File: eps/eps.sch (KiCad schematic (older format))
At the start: 0 parts

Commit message: fourteen mosfets
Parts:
- added H1: EPS Stack Header 2, symbol Connector_Generic:Conn_02x26_Odd_Even
- added H2: EPS Stack Header 1, symbol Connector_Generic:Conn_02x26_Odd_Even
- added Q1, Q10, Q11, Q12, Q13, Q14, Q2, Q3, Q4, Q5, Q6, Q7, Q8, Q9: IRF7404, Package_SO:SOIC-8_3.9x4.9mm_P1.27mm, symbol Transistor_FET:IRF7404
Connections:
- net +12V: now also Q1.5 (D), Q1.6 (D), Q1.7 (D), Q1.8 (D), Q14.5 (D), Q14.6 (D), Q14.7 (D), Q14.8 (D), Q2.5 (D), Q2.6 (D), Q2.7 (D), Q2.8 (D)
- net +3V3: now also Q10.5 (D), Q10.6 (D), Q10.7 (D), Q10.8 (D), Q11.5 (D), Q11.6 (D), Q11.7 (D), Q11.8 (D), Q8.5 (D), Q8.6 (D), Q8.7 (D), Q8.8 (D), Q9.5 (D), Q9.6 (D), Q9.7 (D), Q9.8 (D)
- net +5V: now also Q12.5 (D), Q12.6 (D), Q12.7 (D), Q12.8 (D), Q5.5 (D), Q5.6 (D), Q5.7 (D), Q5.8 (D), Q6.5 (D), Q6.6 (D), Q6.7 (D), Q6.8 (D), Q7.5 (D), Q7.6 (D), Q7.7 (D), Q7.8 (D)
- net +BATT: now also Q13.5 (D), Q13.6 (D), Q13.7 (D), Q13.8 (D), Q3.5 (D), Q3.6 (D), Q3.7 (D), Q3.8 (D), Q4.5 (D), Q4.6 (D), Q4.7 (D), Q4.8 (D)
- net GND: now also H2.14 (Pin_14), H2.17 (Pin_17), H2.21 (Pin_21), H2.22 (Pin_22), H2.29 (Pin_29), H2.30 (Pin_30), H2.32 (Pin_32), H2.47 (Pin_47), H2.48 (Pin_48), H2.9 (Pin_9)
- new net 12VBUS: H2.23 (Pin_23), H2.24 (Pin_24), Q14.1 (S), Q14.2 (S), Q14.3 (S)
- new net 3V3BUS: H2.27 (Pin_27), H2.28 (Pin_28), Q11.1 (S), Q11.2 (S), Q11.3 (S)
- new net 5VBUS: H2.25 (Pin_25), H2.26 (Pin_26), Q12.1 (S), Q12.2 (S), Q12.3 (S)
- new net 5VUSBCHG: H1.32 (Pin_32)
- new net BATTBUS: H2.45 (Pin_45), H2.46 (Pin_46), Q13.1 (S), Q13.2 (S), Q13.3 (S)
- new net BCR_OUT: H2.41 (Pin_41), H2.42 (Pin_42), H2.43 (Pin_43), H2.44 (Pin_44)
- new net BUS12SIG: Q14.4 (G)
- new net BUS3SIG: Q11.4 (G)
- new net BUS5SIG: Q12.4 (G)
- new net BUSBSIG: Q13.4 (G)
- new net PCM_IN: H2.35 (Pin_35), H2.36 (Pin_36)
- new net SCL: H1.43 (Pin_43)
- new net SDA: H1.41 (Pin_41)
- new net SIG1: Q1.4 (G)
- new net SIG10: Q10.4 (G)
- new net SIG2: Q2.4 (G)
- new net SIG3: Q3.4 (G)
- new net SIG4: Q4.4 (G)
- new net SIG5: Q5.4 (G)
- new net SIG6: Q6.4 (G)
- new net SIG7: Q7.4 (G)
- new net SIG8: Q8.4 (G)
- new net SIG9: Q9.4 (G)
- new net SW1: H2.8 (Pin_8), Q1.1 (S), Q1.2 (S), Q1.3 (S)
- new net SW10: H2.20 (Pin_20), Q10.1 (S), Q10.2 (S), Q10.3 (S)
- new net SW2: H2.10 (Pin_10), Q2.1 (S), Q2.2 (S), Q2.3 (S)
- new net SW3: H2.11 (Pin_11), Q3.1 (S), Q3.2 (S), Q3.3 (S)
- new net SW4: H2.12 (Pin_12), Q4.1 (S), Q4.2 (S), Q4.3 (S)
- new net SW5: H2.13 (Pin_13), Q5.1 (S), Q5.2 (S), Q5.3 (S)
- new net SW6: H2.15 (Pin_15), Q6.1 (S), Q6.2 (S), Q6.3 (S)
- new net SW7: H2.16 (Pin_16), Q7.1 (S), Q7.2 (S), Q7.3 (S)
- new net SW8: H2.18 (Pin_18), Q8.1 (S), Q8.2 (S), Q8.3 (S)
- new net SW9: H2.19 (Pin_19), Q9.1 (S), Q9.2 (S), Q9.3 (S)
- no-connect marks 0 -> 67
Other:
- note added: "FOURTEEN MOSFETS!!!!!"

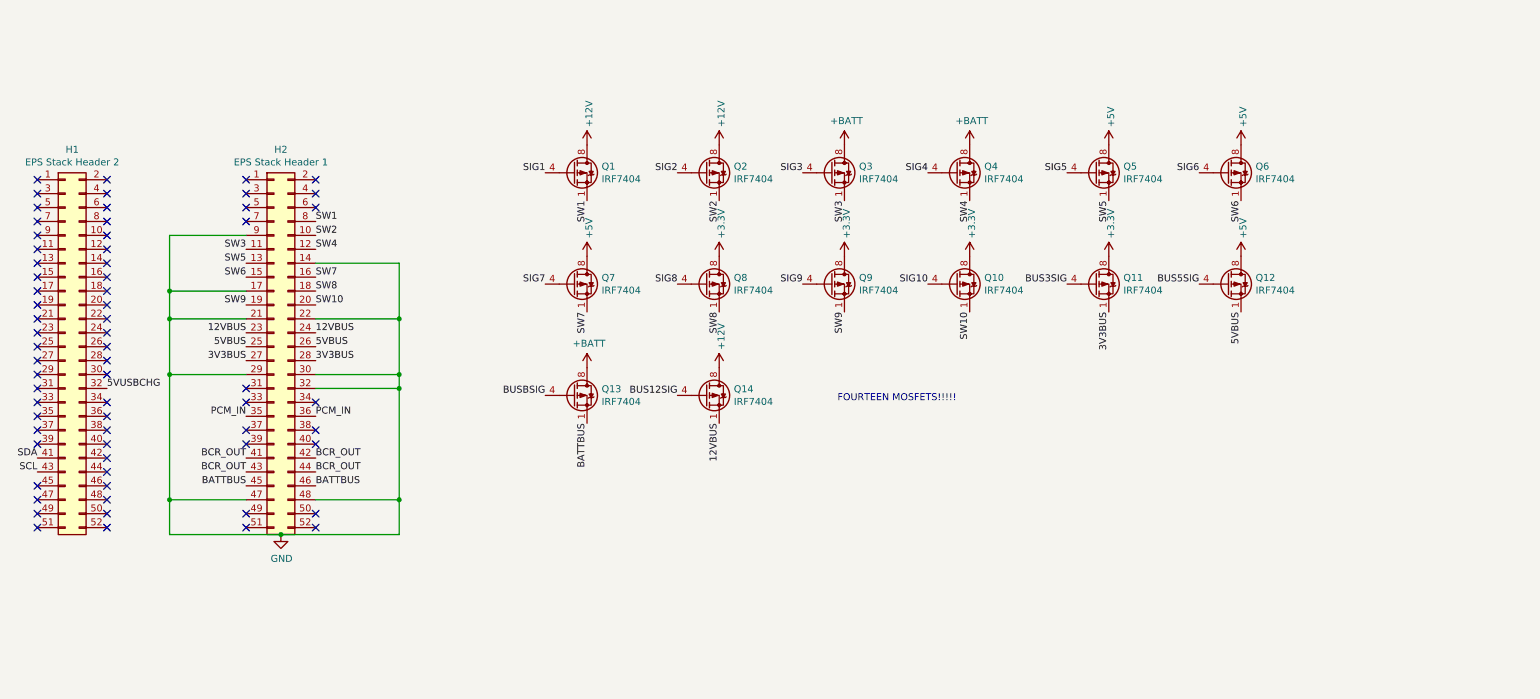
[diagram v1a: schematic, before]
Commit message: 24 mosfets
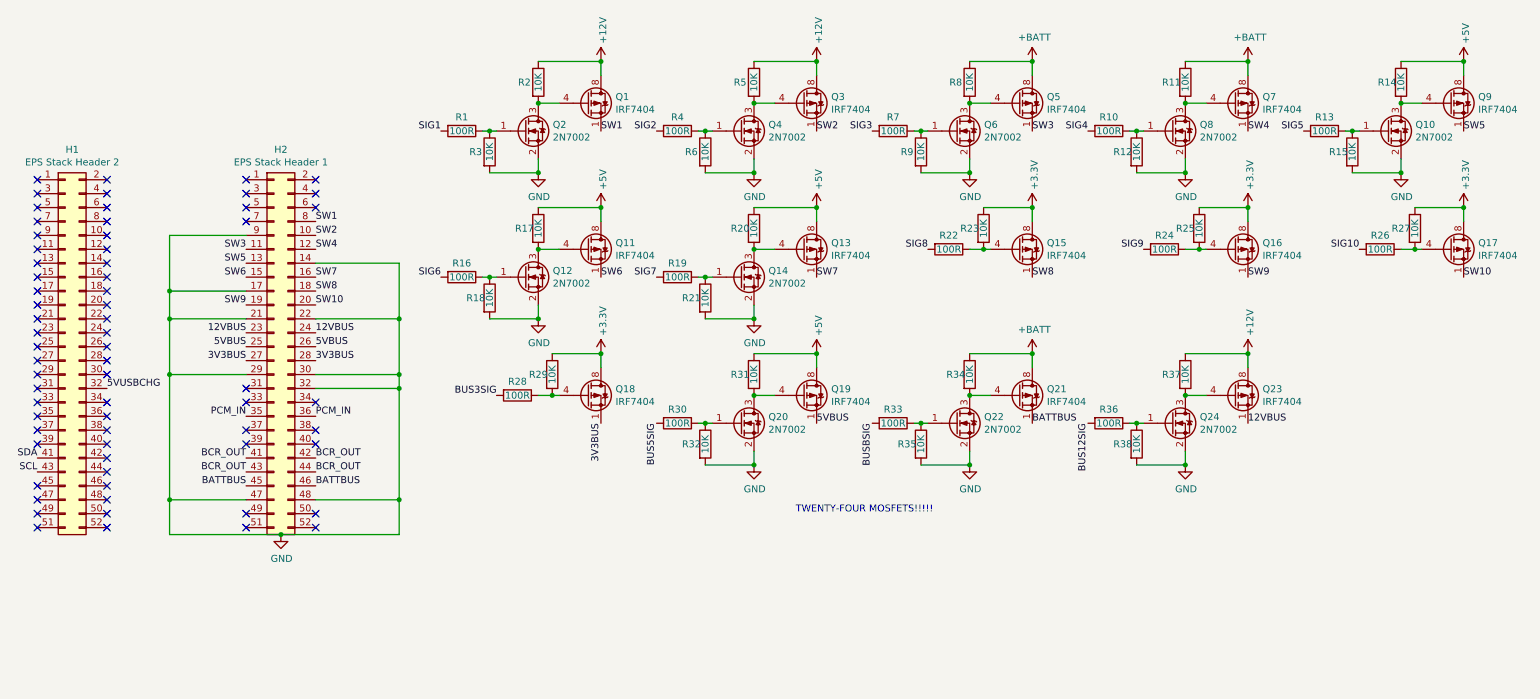
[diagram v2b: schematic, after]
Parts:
- removed Q10, Q12, Q14, Q2, Q4, Q6, Q8: IRF7404, Package_SO:SOIC-8_3.9x4.9mm_P1.27mm, symbol Transistor_FET:IRF7404
- added Q10, Q12, Q14, Q2, Q20, Q22, Q24, Q4, Q6, Q8: 2N7002, Package_TO_SOT_SMD:SOT-23, symbol Transistor_FET:2N7002
- added Q11, Q15, Q16, Q17, Q19, Q21, Q23: IRF7404, Package_SO:SOIC-8_3.9x4.9mm_P1.27mm, symbol Transistor_FET:IRF7404
- added R1, R10, R13, R16, R19, R22, R24, R26, R28, R30, R33, R36, R4, R7: 100R, symbol Device:R
- added R11, R12, R14, R15, R17, R18, R2, R20, R21, R23, R25, R27, R29, R3, R31, R32, R34, R35, R37, R38, R5, R6, R8, R9: 10K, symbol Device:R
- renumbered Q11 to Q18
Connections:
- net +12V: now also Q3.5 (D), Q3.6 (D), Q3.7 (D), Q3.8 (D), Q23.5 (D), Q23.6 (D), Q23.7 (D), Q23.8 (D), R2.1, R37.1, R5.1
- net +3V3: now also Q15.5 (D), Q15.6 (D), Q15.7 (D), Q15.8 (D), Q16.5 (D), Q16.6 (D), Q16.7 (D), Q16.8 (D), Q17.5 (D), Q17.6 (D), Q17.7 (D), Q17.8 (D), R23.1, R25.1, R27.1, R29.1; no longer Q9.5 (D), Q9.6 (D), Q9.7 (D), Q9.8 (D)
- net +5V: now also Q13.5 (D), Q13.6 (D), Q13.7 (D), Q13.8 (D), Q9.5 (D), Q9.6 (D), Q9.7 (D), Q9.8 (D), Q11.5 (D), Q11.6 (D), Q11.7 (D), Q11.8 (D), Q19.5 (D), Q19.6 (D), Q19.7 (D), Q19.8 (D), R14.1, R17.1, R20.1, R31.1; no longer Q5.5 (D), Q5.6 (D), Q5.7 (D), Q5.8 (D), Q7.5 (D), Q7.6 (D), Q7.7 (D), Q7.8 (D)
- net +BATT: now also Q5.5 (D), Q5.6 (D), Q5.7 (D), Q5.8 (D), Q7.5 (D), Q7.6 (D), Q7.7 (D), Q7.8 (D), Q21.5 (D), Q21.6 (D), Q21.7 (D), Q21.8 (D), R11.1, R34.1, R8.1; no longer Q13.5 (D), Q13.6 (D), Q13.7 (D), Q13.8 (D), Q3.5 (D), Q3.6 (D), Q3.7 (D), Q3.8 (D)
- net 12VBUS: now also Q23.1 (S), Q23.2 (S), Q23.3 (S)
- net 5VBUS: now also Q19.1 (S), Q19.2 (S), Q19.3 (S)
- net BATTBUS: now also Q21.1 (S), Q21.2 (S), Q21.3 (S); no longer Q13.1 (S), Q13.2 (S), Q13.3 (S)
- net BUS12SIG: now also R36.2
- net BUS3SIG: now also R28.2; no longer Q18.4 (G)
- net BUS5SIG: now also R30.2
- net BUSBSIG: now also R33.2; no longer Q13.4 (G)
- net GND: now also Q10.2 (S), Q12.2 (S), Q14.2 (S), Q2.2 (S), Q20.2 (S), Q22.2 (S), Q24.2 (S), Q4.2 (S), Q6.2 (S), Q8.2 (S), R12.2, R15.2, R18.2, R21.2, R3.2, R32.2, R35.2, R38.2, R6.2, R9.2
- net SIG1: now also R1.2; no longer Q1.4 (G)
- net SIG10: now also R26.2
- net SIG2: now also R4.2
- net SIG3: now also R7.2; no longer Q3.4 (G)
- net SIG4: now also R10.2
- net SIG5: now also R13.2; no longer Q5.4 (G)
- net SIG6: now also R16.2
- net SIG7: now also R19.2; no longer Q7.4 (G)
- net SIG8: now also R22.2
- net SIG9: now also R24.2; no longer Q9.4 (G)
- net SW10: now also Q17.1 (S), Q17.2 (S), Q17.3 (S)
- net SW2: now also Q3.1 (S), Q3.2 (S), Q3.3 (S)
- net SW3: now also Q5.1 (S), Q5.2 (S), Q5.3 (S); no longer Q3.1 (S), Q3.2 (S), Q3.3 (S)
- net SW4: now also Q7.1 (S), Q7.2 (S), Q7.3 (S)
- net SW5: now also Q9.1 (S), Q9.2 (S), Q9.3 (S); no longer Q5.1 (S), Q5.2 (S), Q5.3 (S)
- net SW6: now also Q11.1 (S), Q11.2 (S), Q11.3 (S)
- net SW7: now also Q13.1 (S), Q13.2 (S), Q13.3 (S); no longer Q7.1 (S), Q7.2 (S), Q7.3 (S)
- net SW8: now also Q15.1 (S), Q15.2 (S), Q15.3 (S)
- net SW9: now also Q16.1 (S), Q16.2 (S), Q16.3 (S); no longer Q9.1 (S), Q9.2 (S), Q9.3 (S)
- new net: Q2.1 (G), R1.1, R3.1
- new net: Q1.4 (G), Q2.3 (D), R2.2
- new net: Q18.4 (G), R28.1, R29.2
- new net: Q4.1 (G), R4.1, R6.1
- new net: Q3.4 (G), Q4.3 (D), R5.2
- new net: Q6.1 (G), R7.1, R9.1
- new net: Q5.4 (G), Q6.3 (D), R8.2
- new net: Q8.1 (G), R10.1, R12.1
- new net: Q7.4 (G), Q8.3 (D), R11.2
- new net: Q10.1 (G), R13.1, R15.1
- new net: Q10.3 (D), Q9.4 (G), R14.2
- new net: Q12.1 (G), R16.1, R18.1
- new net: Q11.4 (G), Q12.3 (D), R17.2
- new net: Q14.1 (G), R19.1, R21.1
- new net: Q13.4 (G), Q14.3 (D), R20.2
- new net: Q15.4 (G), R22.1, R23.2
- new net: Q16.4 (G), R24.1, R25.2
- new net: Q17.4 (G), R26.1, R27.2
- new net: Q20.1 (G), R30.1, R32.1
- new net: Q19.4 (G), Q20.3 (D), R31.2
- new net: Q22.1 (G), R33.1, R35.1
- new net: Q21.4 (G), Q22.3 (D), R34.2
- new net: Q24.1 (G), R36.1, R38.1
- new net: Q23.4 (G), Q24.3 (D), R37.2
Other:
- note added: "TWENTY-FOUR MOSFETS!!!!!"
- note removed: "FOURTEEN MOSFETS!!!!!"
- moved on the sheet: Q1, Q18

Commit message: correct p channel orientation, bias bus to be on with no input
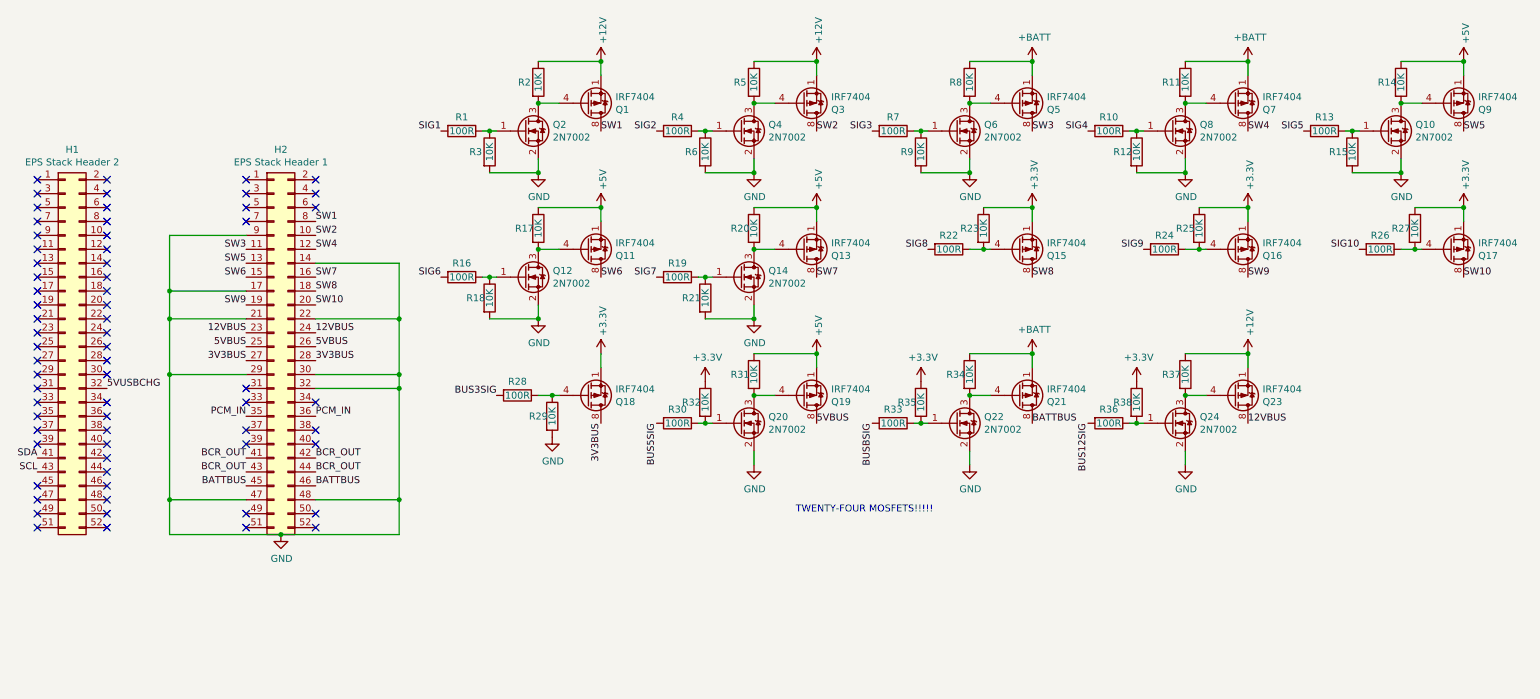
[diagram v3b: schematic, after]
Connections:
- net +12V: now also Q1.1 (S), Q1.2 (S), Q1.3 (S), Q23.1 (S), Q23.2 (S), Q23.3 (S), Q3.1 (S), Q3.2 (S), Q3.3 (S); no longer Q1.5 (D), Q1.6 (D), Q1.7 (D), Q1.8 (D), Q23.5 (D), Q23.6 (D), Q23.7 (D), Q23.8 (D), Q3.5 (D), Q3.6 (D), Q3.7 (D), Q3.8 (D)
- net +3V3: now also Q15.1 (S), Q15.2 (S), Q15.3 (S), Q16.1 (S), Q16.2 (S), Q16.3 (S), Q17.1 (S), Q17.2 (S), Q17.3 (S), Q18.1 (S), Q18.2 (S), Q18.3 (S), R32.1, R35.1, R38.1; no longer Q15.5 (D), Q15.6 (D), Q15.7 (D), Q15.8 (D), Q16.5 (D), Q16.6 (D), Q16.7 (D), Q16.8 (D), Q17.5 (D), Q17.6 (D), Q17.7 (D), Q17.8 (D), Q18.5 (D), Q18.6 (D), Q18.7 (D), Q18.8 (D), R29.1
- net +5V: now also Q11.1 (S), Q11.2 (S), Q11.3 (S), Q13.1 (S), Q13.2 (S), Q13.3 (S), Q19.1 (S), Q19.2 (S), Q19.3 (S), Q9.1 (S), Q9.2 (S), Q9.3 (S); no longer Q11.5 (D), Q11.6 (D), Q11.7 (D), Q11.8 (D), Q13.5 (D), Q13.6 (D), Q13.7 (D), Q13.8 (D), Q19.5 (D), Q19.6 (D), Q19.7 (D), Q19.8 (D), Q9.5 (D), Q9.6 (D), Q9.7 (D), Q9.8 (D)
- net +BATT: now also Q21.1 (S), Q21.2 (S), Q21.3 (S), Q5.1 (S), Q5.2 (S), Q5.3 (S), Q7.1 (S), Q7.2 (S), Q7.3 (S); no longer Q21.5 (D), Q21.6 (D), Q21.7 (D), Q21.8 (D), Q5.5 (D), Q5.6 (D), Q5.7 (D), Q5.8 (D), Q7.5 (D), Q7.6 (D), Q7.7 (D), Q7.8 (D)
- net 12VBUS: now also Q23.5 (D), Q23.6 (D), Q23.7 (D), Q23.8 (D); no longer Q23.1 (S), Q23.2 (S), Q23.3 (S)
- net 3V3BUS: now also Q18.5 (D), Q18.6 (D), Q18.7 (D), Q18.8 (D); no longer Q18.1 (S), Q18.2 (S), Q18.3 (S)
- net 5VBUS: now also Q19.5 (D), Q19.6 (D), Q19.7 (D), Q19.8 (D); no longer Q19.1 (S), Q19.2 (S), Q19.3 (S)
- net BATTBUS: now also Q21.5 (D), Q21.6 (D), Q21.7 (D), Q21.8 (D); no longer Q21.1 (S), Q21.2 (S), Q21.3 (S)
- net GND: now also R29.2; no longer R32.2, R35.2, R38.2
- net SW1: now also Q1.5 (D), Q1.6 (D), Q1.7 (D), Q1.8 (D); no longer Q1.1 (S), Q1.2 (S), Q1.3 (S)
- net SW10: now also Q17.5 (D), Q17.6 (D), Q17.7 (D), Q17.8 (D); no longer Q17.1 (S), Q17.2 (S), Q17.3 (S)
- net SW2: now also Q3.5 (D), Q3.6 (D), Q3.7 (D), Q3.8 (D); no longer Q3.1 (S), Q3.2 (S), Q3.3 (S)
- net SW3: now also Q5.5 (D), Q5.6 (D), Q5.7 (D), Q5.8 (D); no longer Q5.1 (S), Q5.2 (S), Q5.3 (S)
- net SW4: now also Q7.5 (D), Q7.6 (D), Q7.7 (D), Q7.8 (D); no longer Q7.1 (S), Q7.2 (S), Q7.3 (S)
- net SW5: now also Q9.5 (D), Q9.6 (D), Q9.7 (D), Q9.8 (D); no longer Q9.1 (S), Q9.2 (S), Q9.3 (S)
- net SW6: now also Q11.5 (D), Q11.6 (D), Q11.7 (D), Q11.8 (D); no longer Q11.1 (S), Q11.2 (S), Q11.3 (S)
- net SW7: now also Q13.5 (D), Q13.6 (D), Q13.7 (D), Q13.8 (D); no longer Q13.1 (S), Q13.2 (S), Q13.3 (S)
- net SW8: now also Q15.5 (D), Q15.6 (D), Q15.7 (D), Q15.8 (D); no longer Q15.1 (S), Q15.2 (S), Q15.3 (S)
- net SW9: now also Q16.5 (D), Q16.6 (D), Q16.7 (D), Q16.8 (D); no longer Q16.1 (S), Q16.2 (S), Q16.3 (S)
- net at Q18.4 (G), R28.1: now also R29.1; no longer R29.2
- net at Q20.1 (G), R30.1: now also R32.2; no longer R32.1
- net at Q22.1 (G), R33.1: now also R35.2; no longer R35.1
- net at Q24.1 (G), R36.1: now also R38.2; no longer R38.1
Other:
- moved on the sheet: R29, R32, R35, R38
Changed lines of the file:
@@
 F 3 "http://www.infineon.com/dgdl/irf7404.pdf?fileId=5546d462533600a4015355fa2b5b1b9e" V 4700 3200 50  0001 L CNN
 	1    4700 3200
-	1    0    0    -1
+	1    0    0    1
 $EndComp
 Text Label 3650 1300 2    50   ~ 0
@@
 F 3 "http://www.infineon.com/dgdl/irf7404.pdf?fileId=5546d462533600a4015355fa2b5b1b9e" V 4700 1100 50  0001 L CNN
 	1    4700 1100
-	1    0    0    -1
+	1    0    0    1
 $EndComp
 $Comp
@@
 F 3 "http://www.infineon.com/dgdl/irf7404.pdf?fileId=5546d462533600a4015355fa2b5b1b9e" V 6250 1100 50  0001 L CNN
 	1    6250 1100
-	1    0    0    -1
+	1    0    0    1
 $EndComp
 $Comp
@@
 F 3 "http://www.infineon.com/dgdl/irf7404.pdf?fileId=5546d462533600a4015355fa2b5b1b9e" V 7800 1100 50  0001 L CNN
 	1    7800 1100
-	1    0    0    -1
+	1    0    0    1
 $EndComp
 $Comp
@@
 F 3 "http://www.infineon.com/dgdl/irf7404.pdf?fileId=5546d462533600a4015355fa2b5b1b9e" V 9350 1100 50  0001 L CNN
 	1    9350 1100
-	1    0    0    -1
+	1    0    0    1
 $EndComp
 $Comp
@@
 F 3 "http://www.infineon.com/dgdl/irf7404.pdf?fileId=5546d462533600a4015355fa2b5b1b9e" V 10900 1100 50  0001 L CNN
 	1    10900 1100
-	1    0    0    -1
+	1    0    0    1
 $EndComp
 $Comp
@@
 F 3 "http://www.infineon.com/dgdl/irf7404.pdf?fileId=5546d462533600a4015355fa2b5b1b9e" V 4700 2150 50  0001 L CNN
 	1    4700 2150
-	1    0    0    -1
+	1    0    0    1
 $EndComp
 $Comp
@@
 F 3 "http://www.infineon.com/dgdl/irf7404.pdf?fileId=5546d462533600a4015355fa2b5b1b9e" V 6250 2150 50  0001 L CNN
 	1    6250 2150
-	1    0    0    -1
+	1    0    0    1
 $EndComp
 $Comp
@@
 F 3 "http://www.infineon.com/dgdl/irf7404.pdf?fileId=5546d462533600a4015355fa2b5b1b9e" V 7800 2150 50  0001 L CNN
 	1    7800 2150
-	1    0    0    -1
+	1    0    0    1
 $EndComp
 Wire Wire Line
@@
 F 3 "http://www.infineon.com/dgdl/irf7404.pdf?fileId=5546d462533600a4015355fa2b5b1b9e" V 9350 2150 50  0001 L CNN
 	1    9350 2150
-	1    0    0    -1
+	1    0    0    1
 $EndComp
 Wire Wire Line
@@
 F 3 "http://www.infineon.com/dgdl/irf7404.pdf?fileId=5546d462533600a4015355fa2b5b1b9e" V 10900 2150 50  0001 L CNN
 	1    10900 2150
-	1    0    0    -1
+	1    0    0    1
 $EndComp
 Wire Wire Line
@@
 L Device:R R29
 U 1 1 6191C4AE
-P 4450 3050
-F 0 "R29" H 4350 3050 50  0000 C CNN
-F 1 "10K" V 4450 3050 50  0000 C CNN
-F 2 "" V 4380 3050 50  0001 C CNN
-F 3 "~" H 4450 3050 50  0001 C CNN
-	1    4450 3050
-	1    0    0    -1
-$EndComp
-Wire Wire Line
-	4450 2900 4800 2900
+P 4450 3350
+F 0 "R29" H 4350 3350 50  0000 C CNN
+F 1 "10K" V 4450 3350 50  0000 C CNN
+F 2 "" V 4380 3350 50  0001 C CNN
+F 3 "~" H 4450 3350 50  0001 C CNN
+	1    4450 3350
+	1    0    0    -1
+$EndComp
 Wire Wire Line
 	4350 3200 4450 3200
@@
 Wire Wire Line
 	4800 2900 4800 3000
-Connection ~ 4800 2900
 $Comp
 L Device:R R30
@@
 F 3 "http://www.infineon.com/dgdl/irf7404.pdf?fileId=5546d462533600a4015355fa2b5b1b9e" V 6250 3200 50  0001 L CNN
 	1    6250 3200
-	1    0    0    -1
+	1    0    0    1
 $EndComp
 $Comp
@@
 L Device:R R32
 U 1 1 61927005
-P 5550 3550
-F 0 "R32" H 5450 3550 50  0000 C CNN
-F 1 "10K" V 5550 3550 50  0000 C CNN
-F 2 "" V 5480 3550 50  0001 C CNN
-F 3 "~" H 5550 3550 50  0001 C CNN
-	1    5550 3550
-	1    0    0    -1
-$EndComp
-Wire Wire Line
-	5550 3700 5900 3700
+P 5550 3250
+F 0 "R32" H 5450 3250 50  0000 C CNN
+F 1 "10K" V 5550 3250 50  0000 C CNN
+F 2 "" V 5480 3250 50  0001 C CNN
+F 3 "~" H 5550 3250 50  0001 C CNN
+	1    5550 3250
+	1    0    0    -1
+$EndComp
 Wire Wire Line
 	5900 3700 5900 3600
-Connection ~ 5900 3700
 Connection ~ 5550 3400
 Wire Wire Line
@@
 F 3 "http://www.infineon.com/dgdl/irf7404.pdf?fileId=5546d462533600a4015355fa2b5b1b9e" V 7800 3200 50  0001 L CNN
 	1    7800 3200
-	1    0    0    -1
+	1    0    0    1
 $EndComp
 $Comp
@@
 L Device:R R35
 U 1 1 6193C026
-P 7100 3550
-F 0 "R35" H 7000 3550 50  0000 C CNN
-F 1 "10K" V 7100 3550 50  0000 C CNN
-F 2 "" V 7030 3550 50  0001 C CNN
-F 3 "~" H 7100 3550 50  0001 C CNN
-	1    7100 3550
-	1    0    0    -1
-$EndComp
-Wire Wire Line
-	7100 3700 7450 3700
+P 7100 3250
+F 0 "R35" H 7000 3250 50  0000 C CNN
+F 1 "10K" V 7100 3250 50  0000 C CNN
+F 2 "" V 7030 3250 50  0001 C CNN
+F 3 "~" H 7100 3250 50  0001 C CNN
+	1    7100 3250
+	1    0    0    -1
+$EndComp
 Wire Wire Line
 	7450 3700 7450 3600
-Connection ~ 7450 3700
 Connection ~ 7100 3400
 Wire Wire Line
@@
 F 3 "http://www.infineon.com/dgdl/irf7404.pdf?fileId=5546d462533600a4015355fa2b5b1b9e" V 9350 3200 50  0001 L CNN
 	1    9350 3200
-	1    0    0    -1
+	1    0    0    1
 $EndComp
 $Comp
@@
 L Device:R R38
 U 1 1 61959E02
-P 8650 3550
-F 0 "R38" H 8550 3550 50  0000 C CNN
-F 1 "10K" V 8650 3550 50  0000 C CNN
-F 2 "" V 8580 3550 50  0001 C CNN
-F 3 "~" H 8650 3550 50  0001 C CNN
-	1    8650 3550
-	1    0    0    -1
-$EndComp
-Wire Wire Line
-	8650 3700 9000 3700
+P 8650 3250
+F 0 "R38" H 8550 3250 50  0000 C CNN
+F 1 "10K" V 8650 3250 50  0000 C CNN
+F 2 "" V 8580 3250 50  0001 C CNN
+F 3 "~" H 8650 3250 50  0001 C CNN
+	1    8650 3250
+	1    0    0    -1
+$EndComp
 Wire Wire Line
 	9000 3700 9000 3600
-Connection ~ 9000 3700
 Connection ~ 8650 3400
 Wire Wire Line
 	8650 3400 8700 3400
 Connection ~ 9450 2900
+$Comp
+L power:GND #PWR?
+U 1 1 6176AAEA
+P 4450 3500
+F 0 "#PWR?" H 4450 3250 50  0001 C CNN
+F 1 "GND" H 4455 3327 50  0000 C CNN
+F 2 "" H 4450 3500 50  0001 C CNN
+F 3 "" H 4450 3500 50  0001 C CNN
+	1    4450 3500
+	1    0    0    -1
+$EndComp
+$Comp
+L power:+3.3V #PWR?
+U 1 1 6178C4CA
+P 5550 3100
+F 0 "#PWR?" H 5550 2950 50  0001 C CNN
+F 1 "+3.3V" H 5565 3273 50  0000 C CNN
+F 2 "" H 5550 3100 50  0001 C CNN
+F 3 "" H 5550 3100 50  0001 C CNN
+	1    5550 3100
+	1    0    0    -1
+$EndComp
+$Comp
+L power:+3.3V #PWR?
+U 1 1 6178CD8E
+P 7100 3100
+F 0 "#PWR?" H 7100 2950 50  0001 C CNN
+F 1 "+3.3V" H 7115 3273 50  0000 C CNN
+F 2 "" H 7100 3100 50  0001 C CNN
+F 3 "" H 7100 3100 50  0001 C CNN
+	1    7100 3100
+	1    0    0    -1
+$EndComp
+$Comp
+L power:+3.3V #PWR?
+U 1 1 61790B8A
+P 8650 3100
+F 0 "#PWR?" H 8650 2950 50  0001 C CNN
+F 1 "+3.3V" H 8665 3273 50  0000 C CNN
+F 2 "" H 8650 3100 50  0001 C CNN
+F 3 "" H 8650 3100 50  0001 C CNN
+	1    8650 3100
+	1    0    0    -1
+$EndComp
 $EndSCHEMATC
